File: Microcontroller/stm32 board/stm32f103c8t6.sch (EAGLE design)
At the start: 19 parts, among them J2 796136-1, Q1 8MHz, U1 STM32F103C8T6, X1 32.768KHZ

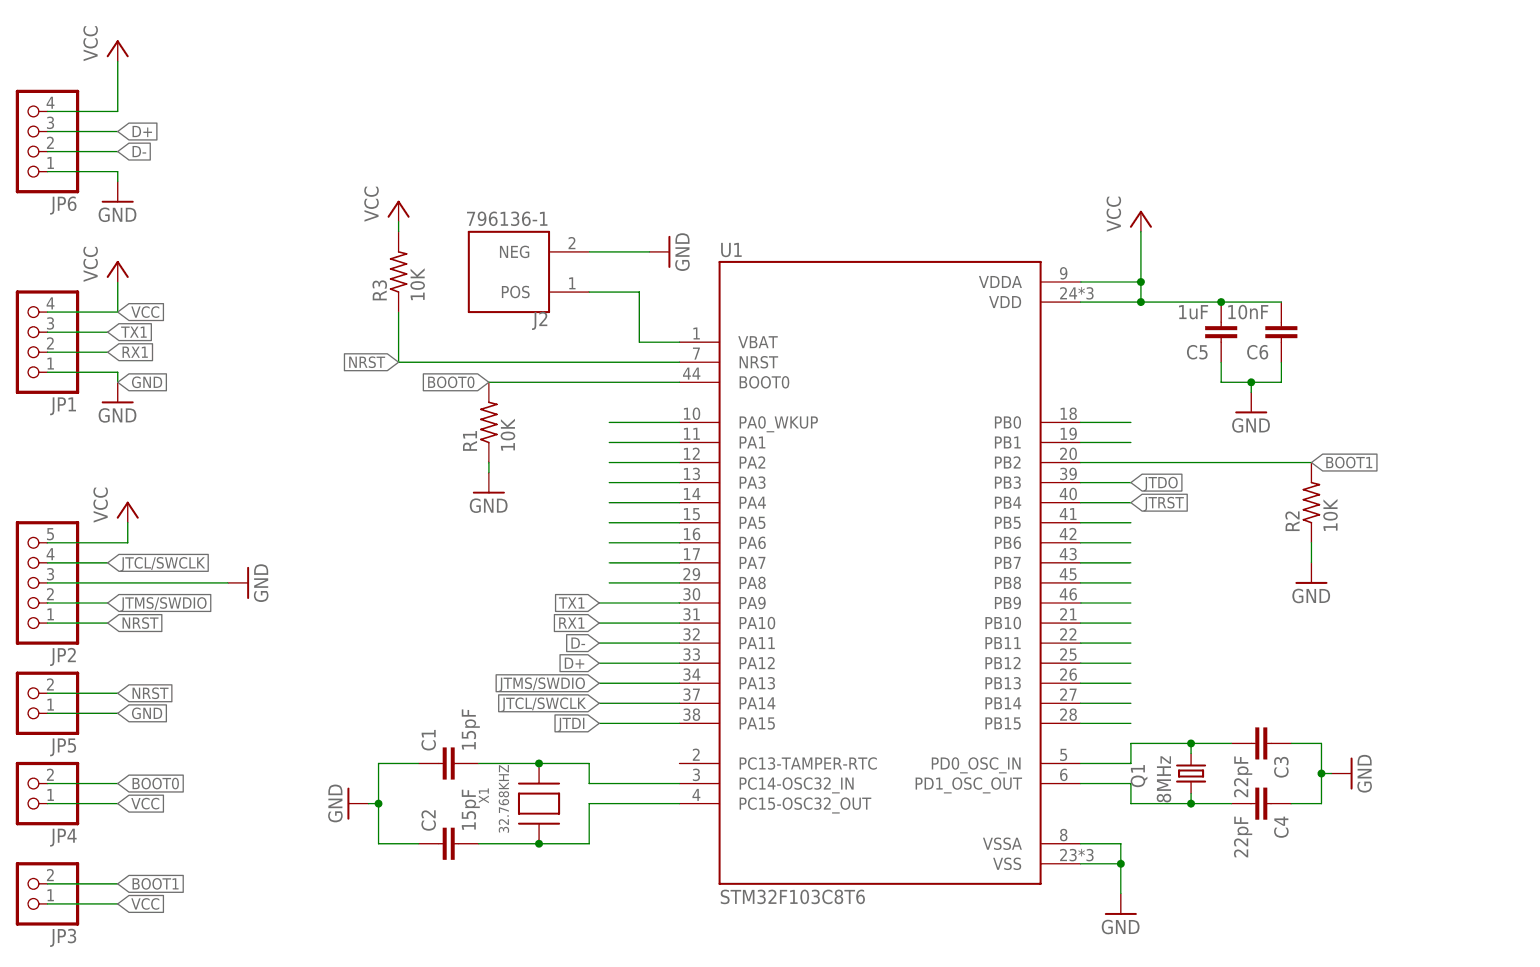
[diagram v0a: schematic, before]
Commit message: added new stm board
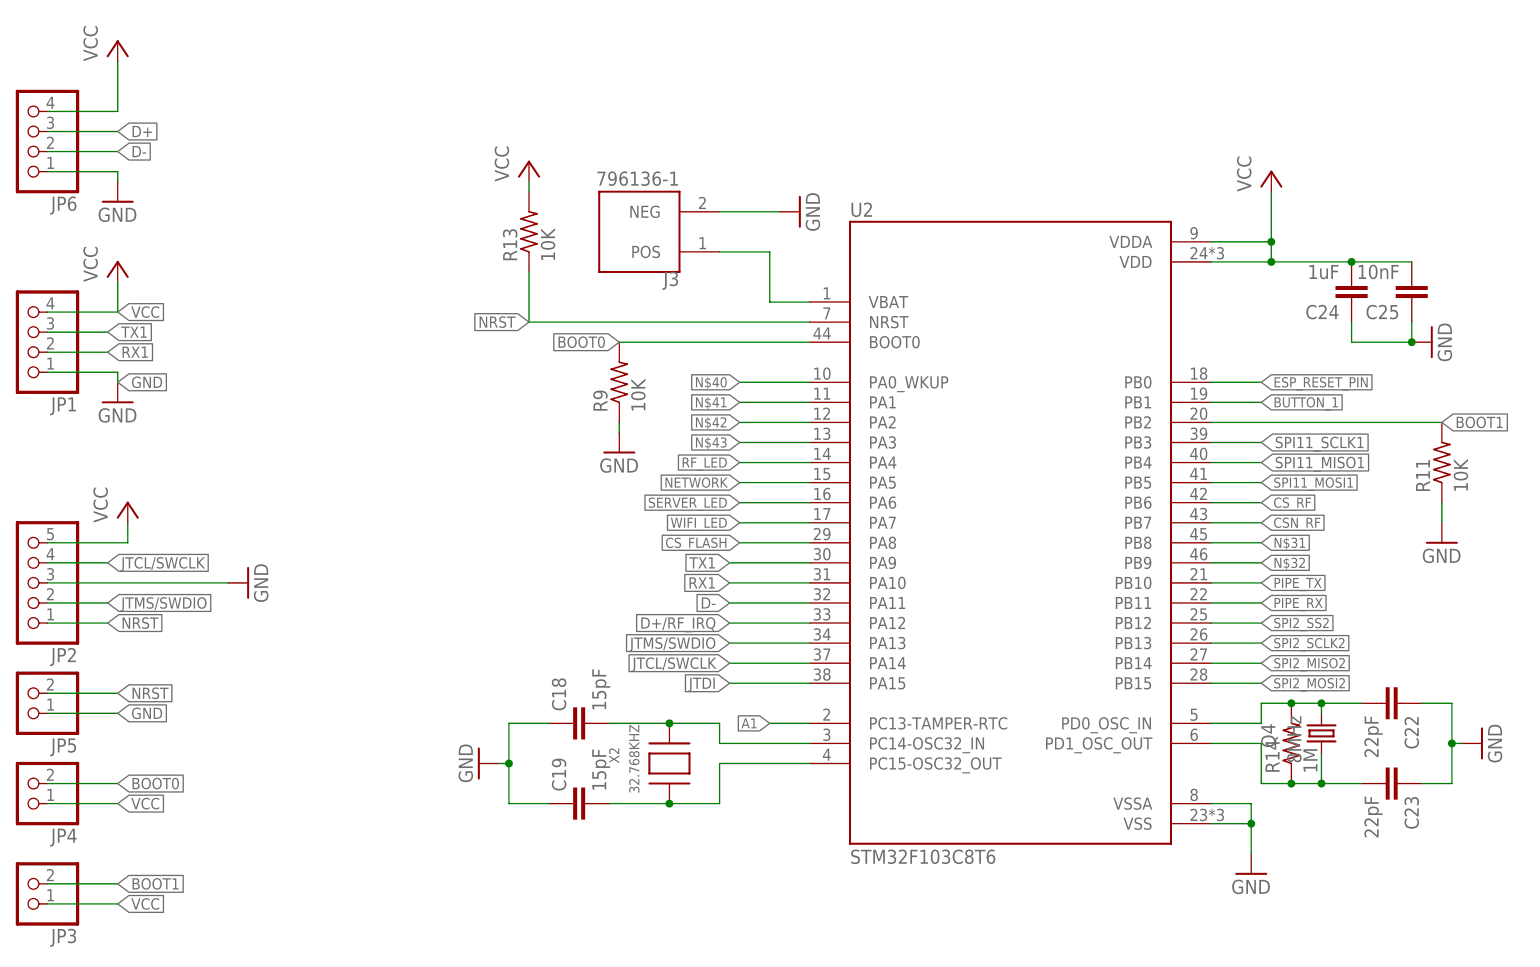
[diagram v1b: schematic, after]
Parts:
- removed C1, C2: 15pF, rcl:C-EUC0603
- removed C3, C4: 22pF, rcl:C-EUC0603
- removed C5: 1uF, rcl:C-EUC0603
- removed C6: 10nF, rcl:C-EUC0603
- removed J2: 796136-1, 796136-1:796136-1
- removed Q1: 8MHz, crystal-geyer_V1_0:KX-7
- removed R1, R2, R3: 10K, rcl:R-US_R0603
- removed U1: STM32F103C8T6, STM32F103C8T6:STM32F103C8T6
- removed X1: 32.768KHZ, adafruit:XTAL-3.2X1.5
- added C18, C19: 15pF, rcl:C-EUC0603
- added C22, C23: 22pF, rcl:C-EUC0603
- added C24: 1uF, rcl:C-EUC0603
- added C25: 10nF, rcl:C-EUC0603
- added J3: 796136-1, 796136-1:796136-1
- added Q4: 8MHz, crystal-geyer_V1_0:KX-7
- added R11, R13, R9: 10K, rcl:R-US_R0603
- added R14: 1M, rcl:R-US_R0603
- added U2: STM32F103C8T6, STM32F103C8T6:STM32F103C8T6
- added X2: 32.768KHZ, adafruit:XTAL-3.2X1.5
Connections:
- removed net JTDO: U1.PB3
- removed net JTRST: U1.PB4
- removed net N$1: C1.2, U1.PC14-OSC32_IN, X1.P$2
- removed net N$11: U1.PB0
- removed net N$12: U1.PB1
- removed net N$13: U1.PA3
- removed net N$14: U1.PA4
- removed net N$15: U1.PB5
- removed net N$16: U1.PB6
- removed net N$17: U1.PB7
- removed net N$18: U1.PB8
- removed net N$19: U1.PB9
- removed net N$2: C2.2, U1.PC15-OSC32_OUT, X1.P$1
- removed net N$20: U1.PB10
- removed net N$21: U1.PB11
- removed net N$22: U1.PB12
- removed net N$23: U1.PB13
- removed net N$24: U1.PB14
- removed net N$25: U1.PB15
- removed net N$26: U1.PA5
- removed net N$27: U1.PA6
- removed net N$28: U1.PA7
- removed net N$29: U1.PA8
- removed net N$3: C4.2, Q1.2, U1.PD1_OSC_OUT
- removed net N$4: C3.2, Q1.1, U1.PD0_OSC_IN
- removed net N$5: J2.POS, U1.VBAT
- removed net N$6: U1.PA0_WKUP
- removed net N$7: U1.PA1
- removed net N$8: U1.PA2
- new net A1: U2.PC13-TAMPER-RTC
- new net BUTTON_1: U2.PB1
- new net CSN_RF: U2.PB7
- new net CS_FLASH: U2.PA8
- new net CS_RF: U2.PB6
- new net D+/RF_IRQ: U2.PA12
- new net ESP_RESET_PIN: U2.PB0
- new net N$10: C19.2, U2.PC15-OSC32_OUT, X2.P$1
- new net N$30: C23.2, Q4.2, R14.1, U2.PD1_OSC_OUT
- new net N$31: C22.2, Q4.1, R14.2, U2.PB8, U2.PD0_OSC_IN
- new net N$32: J3.POS, U2.PB9, U2.VBAT
- new net N$40: U2.PA0_WKUP
- new net N$41: U2.PA1
- new net N$42: U2.PA2
- new net N$43: U2.PA3
- new net N$9: C18.2, U2.PC14-OSC32_IN, X2.P$2
- new net NETWORK: U2.PA5
- new net PIPE_RX: U2.PB11
- new net PIPE_TX: U2.PB10
- new net RF_LED: U2.PA4
- new net SERVER_LED: U2.PA6
- new net SPI11_MISO1: U2.PB4
- new net SPI11_MOSI1: U2.PB5
- new net SPI11_SCLK1: U2.PB3
- new net SPI2_MISO2: U2.PB14
- new net SPI2_MOSI2: U2.PB15
- new net SPI2_SCLK2: U2.PB13
- new net SPI2_SS2: U2.PB12
- new net WIFI_LED: U2.PA7
- net BOOT0: now also R9.2, U2.BOOT0; no longer R1.2, U1.BOOT0
- net BOOT1: now also R11.2, U2.PB2; no longer R2.2, U1.PB2
- net D+: no longer U1.PA12
- net D-: now also U2.PA11; no longer U1.PA11
- net GND: now also C18.1, C19.1, C22.1, C23.1, C24.1, C25.1, J3.NEG, R11.1, R9.1, U2.VSS, U2.VSSA; no longer C1.1, C2.1, C3.1, C4.1, C5.1, C6.1, J2.NEG, R1.1, R2.1, U1.VSS, U1.VSSA
- net JTCL/SWCLK: now also U2.PA14; no longer U1.PA14
- net JTDI: now also U2.PA15; no longer U1.PA15
- net JTMS/SWDIO: now also U2.PA13; no longer U1.PA13
- net NRST: now also R13.1, U2.NRST; no longer R3.1, U1.NRST
- net RX1: now also U2.PA10; no longer U1.PA10
- net TX1: now also U2.PA9; no longer U1.PA9
- net VCC: now also C24.2, C25.2, R13.2, U2.VDD, U2.VDDA; no longer C5.2, C6.2, R3.2, U1.VDD, U1.VDDA
